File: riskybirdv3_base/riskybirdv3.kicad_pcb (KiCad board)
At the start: 4 copper layers, 69.8 x 65 mm, 139 parts, among them IC1 PMW3901MB-TXQT, J10 Conn_01x05, J11 Conn_01x05, J18 Conn_01x05_MountingPin, J19 Conn_01x30_MountingPin, J2 Conn_01x05, J3 Conn_01x02, J4 Conn_01x02, J5 Conn_01x02, J6 Conn_01x02, J7 Conn_01x02, J8 USB_B_Micro, J9 Conn_01x05, Q1 SI2302, Q2 SI2302, Q3 SI2302, Q4 SI2302, SW2 SW_SPST, SW3 SW_SPST, U1 ADS7128IRTER, U10 TLV70018DCKR, U11 TPS54331D, U3 BMI088, U4 MCP73831-2-OT, U6 FT2232HL-REEL, U7 TPS2113A, U9 VL53L1CXV0FY1, Y1 f

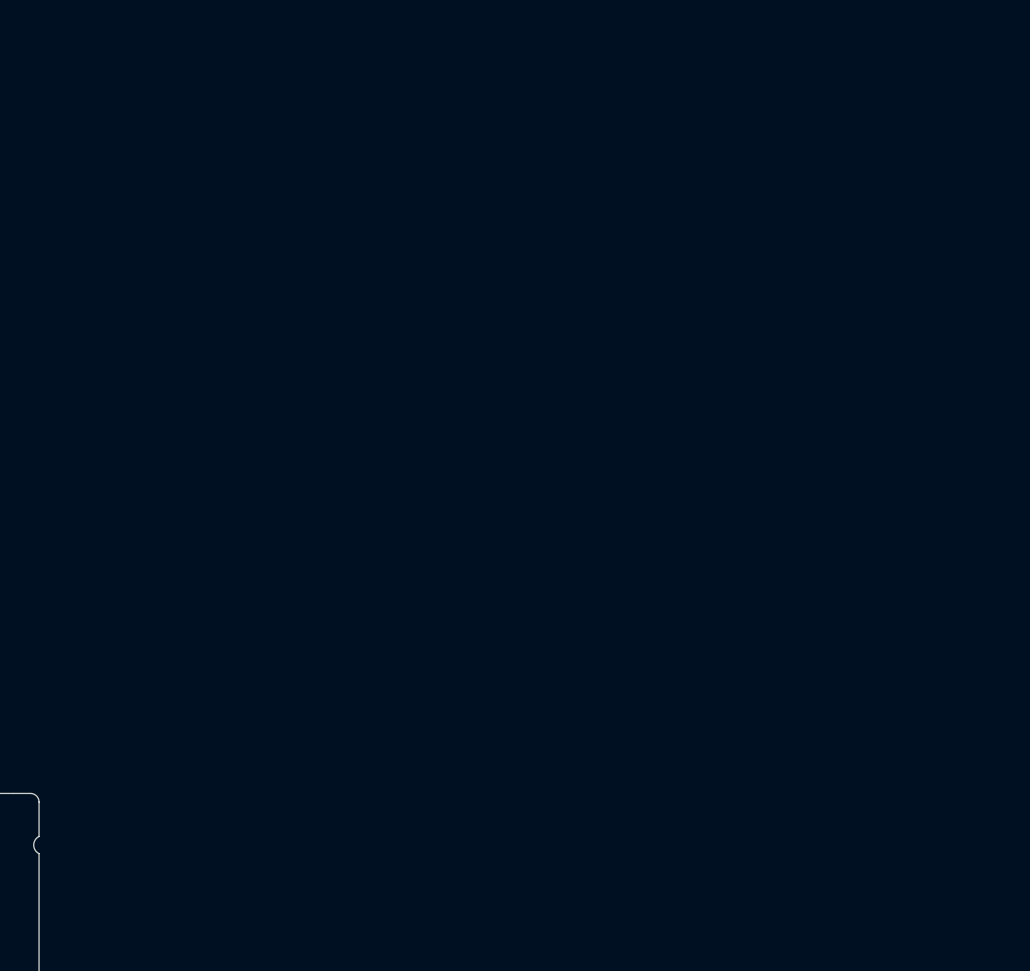
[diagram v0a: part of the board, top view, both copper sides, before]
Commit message: update camera part
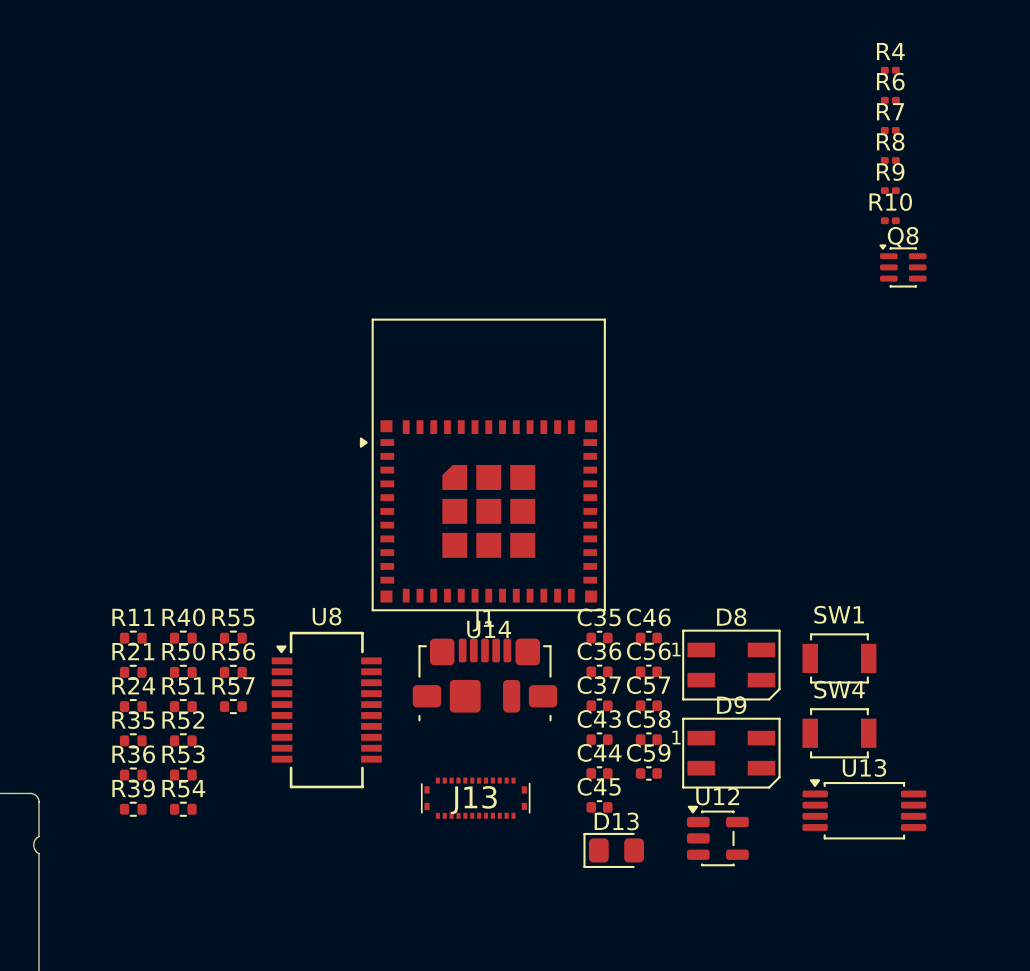
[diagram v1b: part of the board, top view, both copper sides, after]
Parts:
- added C35: 0.1u, Capacitor_SMD:C_0402_1005Metric, F.Cu at (233.4, 58.2)
- added C36: 4.7u, Capacitor_SMD:C_0402_1005Metric, F.Cu at (233.4, 60.1)
- added C37: 0.1u, Capacitor_SMD:C_0402_1005Metric, F.Cu at (233.4, 62.1)
- added C43: 0.1u, Capacitor_SMD:C_0402_1005Metric, F.Cu at (233.4, 64.1)
- added C44: 10n, Capacitor_SMD:C_0402_1005Metric, F.Cu at (233.4, 66.0)
- added C45: 4.7u, Capacitor_SMD:C_0402_1005Metric, F.Cu at (233.4, 68.0)
- added C46: 10u, Capacitor_SMD:C_0402_1005Metric, F.Cu at (236.3, 58.2)
- added C56: 0.1u, Capacitor_SMD:C_0402_1005Metric, F.Cu at (236.3, 60.1)
- added C57: 4.7u, Capacitor_SMD:C_0402_1005Metric, F.Cu at (236.3, 62.1)
- added C58: 0.1u, Capacitor_SMD:C_0402_1005Metric, F.Cu at (236.3, 64.1)
- added C59: 1u, Capacitor_SMD:C_0402_1005Metric, F.Cu at (236.3, 66.0)
- added D13: LED_BLUE, LED_SMD:LED_0805_2012Metric_Pad1.15x1.40mm_HandSolder, F.Cu at (234.4, 70.5)
- added D8: SK6812MINI, LED_SMD:LED_SK6812MINI_PLCC4_3.5x3.5mm_P1.75mm, F.Cu at (241.1, 59.7)
- added D9: SK6812MINI, LED_SMD:LED_SK6812MINI_PLCC4_3.5x3.5mm_P1.75mm, F.Cu at (241.1, 64.9)
- added J1: USB_B_Micro, Connector_USB:USB_Micro-B_Molex_47346-0001, F.Cu at (226.8, 60.4)
- added J13: Conn_02x12_Odd_Even_MountingPin, riskybird:5037762410, F.Cu at (226.2, 67.5)
- added Q8: BC847BDW1, Package_TO_SOT_SMD:SOT-363_SC-70-6, F.Cu at (251.1, 36.6)
- added R10: 10k, Resistor_SMD:R_0201_0603Metric, F.Cu at (250.3, 33.9)
- added R11: 10k, Resistor_SMD:R_0402_1005Metric, F.Cu at (206.3, 58.2)
- added R21: 27, Resistor_SMD:R_0402_1005Metric, F.Cu at (206.3, 60.2)
- added R24: 27, Resistor_SMD:R_0402_1005Metric, F.Cu at (206.3, 62.1)
- added R35: 10k, Resistor_SMD:R_0402_1005Metric, F.Cu at (206.3, 64.1)
- added R36: 10k, Resistor_SMD:R_0402_1005Metric, F.Cu at (206.3, 66.1)
- added R39: 10k, Resistor_SMD:R_0402_1005Metric, F.Cu at (206.3, 68.1)
- added R4: 10k, Resistor_SMD:R_0201_0603Metric, F.Cu at (250.3, 25.1)
- added R40: 10k, Resistor_SMD:R_0402_1005Metric, F.Cu at (209.2, 58.2)
- added R50: 150, Resistor_SMD:R_0402_1005Metric, F.Cu at (209.2, 60.2)
- added R51: 200k, Resistor_SMD:R_0402_1005Metric, F.Cu at (209.2, 62.1)
- added R52: 100k, Resistor_SMD:R_0402_1005Metric, F.Cu at (209.2, 64.1)
- added R53: 10k, Resistor_SMD:R_0402_1005Metric, F.Cu at (209.2, 66.1)
- added R54: 150, Resistor_SMD:R_0402_1005Metric, F.Cu at (209.2, 68.1)
- added R55: 10k, Resistor_SMD:R_0402_1005Metric, F.Cu at (212.2, 58.2)
- added R56: 4.7k, Resistor_SMD:R_0402_1005Metric, F.Cu at (212.2, 60.2)
- added R57: 4.7k, Resistor_SMD:R_0402_1005Metric, F.Cu at (212.2, 62.1)
- added R6: 10k, Resistor_SMD:R_0201_0603Metric, F.Cu at (250.3, 26.9)
- added R7: 10k, Resistor_SMD:R_0201_0603Metric, F.Cu at (250.3, 28.6)
- added R8: 10k, Resistor_SMD:R_0201_0603Metric, F.Cu at (250.3, 30.4)
- added R9: 10k, Resistor_SMD:R_0201_0603Metric, F.Cu at (250.3, 32.1)
- added SW1: SW_SPST, Button_Switch_SMD:SW_SPST_B3U-1000P, F.Cu at (247.4, 59.4)
- added SW4: SW_SPST, Button_Switch_SMD:SW_SPST_B3U-1000P, F.Cu at (247.4, 63.7)
- added U12: LP2985-3.0, Package_TO_SOT_SMD:SOT-23-5, F.Cu at (240.3, 69.8)
- added U13: TPS2113A, Package_SO:TSSOP-8_4.4x3mm_P0.65mm, F.Cu at (248.8, 68.2)
- added U14: ESP32-C6-MINI-1/U, RF_Module:ESP32-C6-MINI-1, F.Cu at (227.0, 50.8)
- added U8: FT231XS, Package_SO:SSOP-20_3.9x8.7mm_P0.635mm, F.Cu at (217.6, 62.4)
